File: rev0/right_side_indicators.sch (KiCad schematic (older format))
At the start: 21 parts, among them IC1 ECP5-BGA256

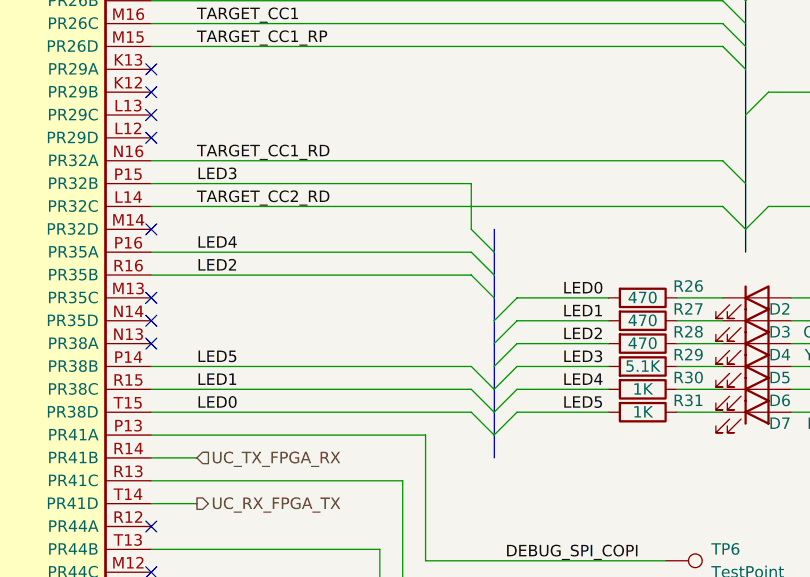
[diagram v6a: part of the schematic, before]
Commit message: hardware: renumber FPGA LEDs
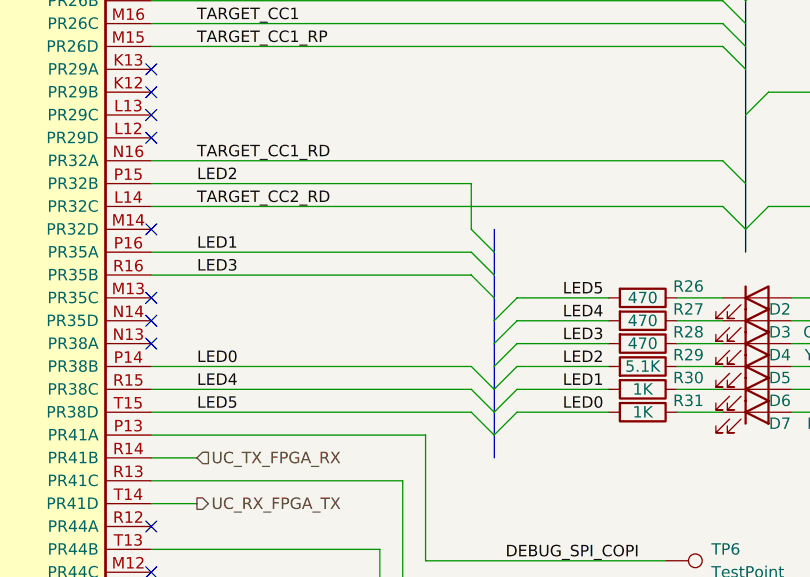
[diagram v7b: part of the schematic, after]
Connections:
- net LED0: now also IC1.P14 (PR38B), R31.2; no longer IC1.T15 (PR38D), R26.2
- net LED1: now also IC1.P16 (PR35A), R30.2; no longer IC1.R15 (PR38C), R27.2
- net LED2: now also IC1.P15 (PR32B), R29.2; no longer IC1.R16 (PR35B), R28.2
- net LED3: now also IC1.R16 (PR35B), R28.2; no longer IC1.P15 (PR32B), R29.2
- net LED4: now also IC1.R15 (PR38C), R27.2; no longer IC1.P16 (PR35A), R30.2
- net LED5: now also IC1.T15 (PR38D), R26.2; no longer IC1.P14 (PR38B), R31.2
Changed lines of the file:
@@
 Sheet 9 9
 Title "LUNA: Right Side I/O"
-Date "2021-01-10"
+Date "2021-01-12"
 Rev "r0"
 Comp "Copyright 2019-2021 Great Scott Gadgets"
@@
 Wire Wire Line
 	3000 4300 4400 4300
-Text Label 3200 3400 0    50   ~ 0
+Text Label 3200 3800 0    50   ~ 0
 LED3
+Text Label 3200 4300 0    50   ~ 0
+LED4
 Text Label 3200 3700 0    50   ~ 0
-LED4
-Text Label 3200 4200 0    50   ~ 0
-LED5
-Text Label 3200 4300 0    50   ~ 0
 LED1
 Entry Wire Line
@@
 	1    0    0    -1
 $EndComp
+Text Label 4800 4300 0    50   ~ 0
+LED1
+Text Label 4800 4200 0    50   ~ 0
+LED2
+Text Label 4800 4100 0    50   ~ 0
+LED3
+Text Label 4800 4000 0    50   ~ 0
+LED4
 Text Label 4800 3900 0    50   ~ 0
-LED0
-Text Label 4800 4000 0    50   ~ 0
-LED1
-Text Label 4800 4100 0    50   ~ 0
-LED2
-Text Label 4800 4200 0    50   ~ 0
-LED3
-Text Label 4800 4300 0    50   ~ 0
-LED4
-Text Label 4800 4400 0    50   ~ 0
 LED5
 Text Label 4550 5450 0    50   ~ 0
@@
 Wire Wire Line
 	3900 5650 3900 5500
-Text Label 3200 4400 0    50   ~ 0
-LED0
-Text Label 3200 3800 0    50   ~ 0
+Text Label 3200 3400 0    50   ~ 0
 LED2
 $Comp
@@
 	0    1    1    0
 $EndComp
-Wire Bus Line
-	5600 1200 5600 3700
-Wire Bus Line
-	4500 3600 4500 4600
 $Comp
 L Device:R R?
@@
 	0    1    1    0
 $EndComp
+Wire Bus Line
+	5600 1200 5600 3700
+Wire Bus Line
+	4500 3600 4500 4600
+Text Label 3200 4400 0    50   ~ 0
+LED5
+Text Label 3200 4200 0    50   ~ 0
+LED0
+Text Label 4800 4400 0    50   ~ 0
+LED0
 $EndSCHEMATC
